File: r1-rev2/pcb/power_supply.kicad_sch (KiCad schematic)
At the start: 28 parts, among them J5 GT-BTP30003-xxxA-16A, Q3 AO3401A, U4 LM66100DCK, U5 TPS62A01DRLR, U6 TPS62A01DRLR, U7 AP2125K-3.0, U8 AP2125K-3.0, U9 TP4057

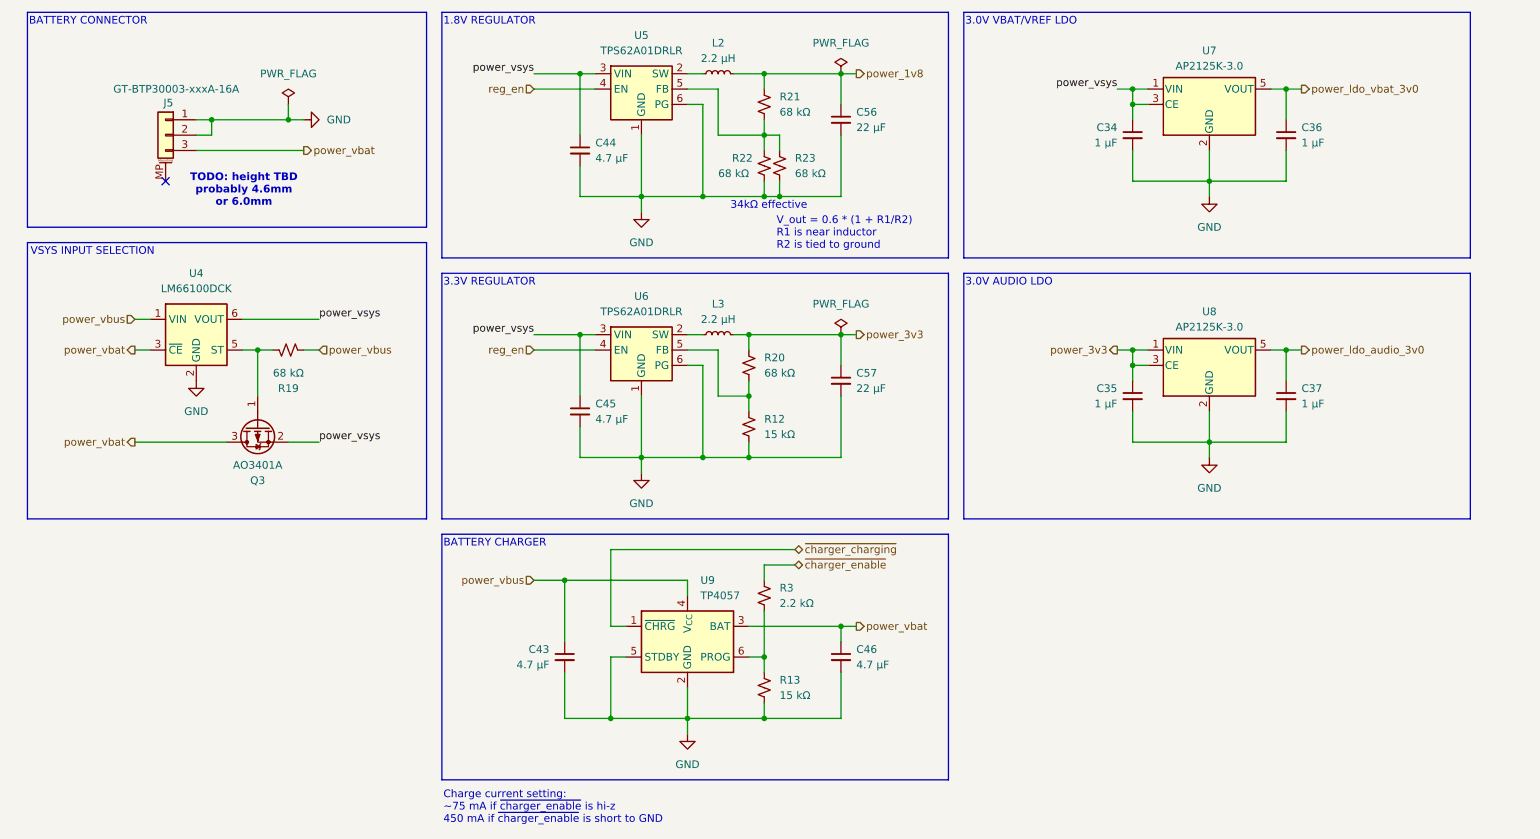
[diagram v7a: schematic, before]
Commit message: R1-Rev2: improve reset circuit, add XSPI CS pullup
Connect NRST to xspi_reset and the regulator power-good signals.
This should ensure that the STM32 and RAM will stay in reset
until both power rails have started up. It shouldn't be necessary
to control xspi_reset with a GPIO, but for now leave it connected
just in case.

The XSPI CS pin also requires an external pullup to guarantee it
will be pulled high during power-on, which is required to ensure
the RAM resets properly.
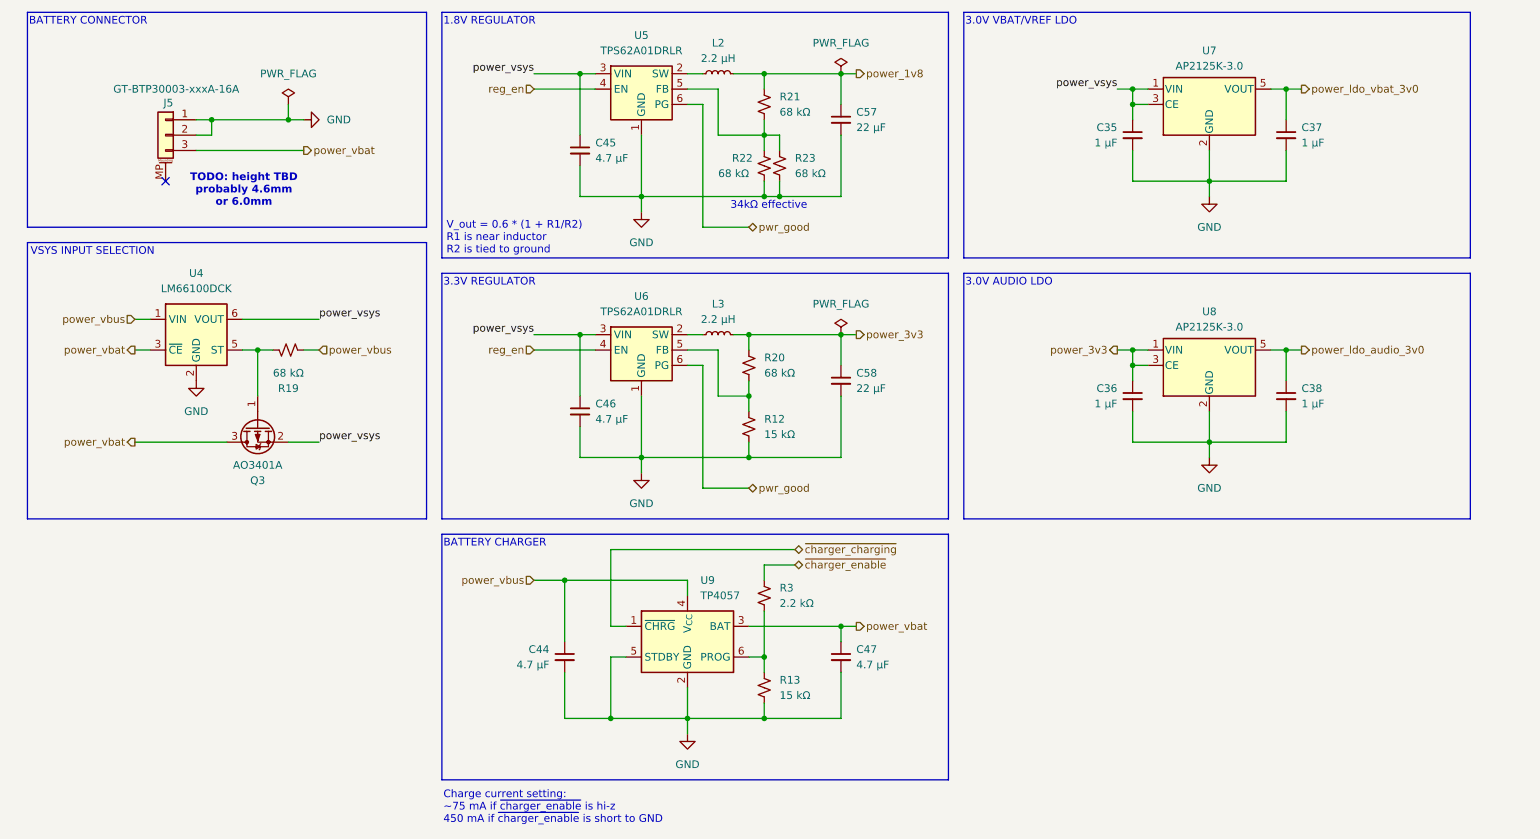
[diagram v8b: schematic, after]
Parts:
- renumbered C34 to C35, C35 to C36, C36 to C37, C37 to C38, C43 to C44, C44 to C45, C45 to C46, C46 to C47, C56 to C57, C57 to C58
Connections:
- net GND: no longer U5.6 (PG), U6.6 (PG)
- new net pwr_good: U5.6 (PG), U6.6 (PG)
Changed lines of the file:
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@@
 	(text "V_out = 0.6 * (1 + R1/R2)\nR1 is near inductor\nR2 is tied to ground"
 		(exclude_from_sim no)
-		(at 154.432 69.596 0)
+		(at 99.822 70.358 0)
 		(effects
 			(font
@@
 	)
 	(junction
-		(at 142.24 63.5)
-		(diameter 0)
-		(color 0 0 0 0)
-	)
-	(junction
-		(at 142.24 106.68)
-		(diameter 0)
-		(color 0 0 0 0)
-	)
-	(junction
 		(at 73.66 50.8)
 		(diameter 0)
@@
 	(wire
 		(pts
-			(xy 142.24 48.26) (xy 142.24 63.5)
-		)
-		(stroke
-			(width 0)
-			(type default)
-		)
-	)
-	(wire
-		(pts
 			(xy 226.06 60.96) (xy 238.76 60.96)
 		)
@@
 	(wire
 		(pts
+			(xy 142.24 91.44) (xy 142.24 111.76)
+		)
+		(stroke
+			(width 0)
+			(type default)
+		)
+	)
+	(wire
+		(pts
 			(xy 139.7 86.36) (xy 142.24 86.36)
 		)
@@
 	(wire
 		(pts
-			(xy 144.78 88.9) (xy 144.78 96.52)
+			(xy 142.24 48.26) (xy 142.24 68.58)
 		)
 		(stroke
@@
 	(wire
 		(pts
-			(xy 132.08 96.52) (xy 132.08 106.68)
+			(xy 144.78 88.9) (xy 144.78 96.52)
 		)
 		(stroke
@@
 	(wire
 		(pts
-			(xy 165.1 86.36) (xy 167.64 86.36)
+			(xy 132.08 96.52) (xy 132.08 106.68)
 		)
 		(stroke
@@
 	(wire
 		(pts
-			(xy 132.08 106.68) (xy 142.24 106.68)
+			(xy 165.1 86.36) (xy 167.64 86.36)
 		)
 		(stroke
@@
 	(wire
 		(pts
-			(xy 139.7 91.44) (xy 142.24 91.44)
+			(xy 132.08 106.68) (xy 149.86 106.68)
 		)
 		(stroke
@@
 	(wire
 		(pts
-			(xy 142.24 91.44) (xy 142.24 106.68)
+			(xy 139.7 91.44) (xy 142.24 91.44)
 		)
 		(stroke
@@
 	(wire
 		(pts
-			(xy 142.24 63.5) (xy 152.4 63.5)
+			(xy 132.08 63.5) (xy 152.4 63.5)
 		)
 		(stroke
@@
 	(wire
 		(pts
+			(xy 142.24 111.76) (xy 149.86 111.76)
+		)
+		(stroke
+			(width 0)
+			(type default)
+		)
+	)
+	(wire
+		(pts
 			(xy 139.7 127) (xy 139.7 129.54)
 		)
@@
 	(wire
 		(pts
-			(xy 142.24 106.68) (xy 149.86 106.68)
-		)
-		(stroke
-			(width 0)
-			(type default)
-		)
-	)
-	(wire
-		(pts
 			(xy 226.06 60.96) (xy 226.06 63.5)
 		)
@@
 	(wire
 		(pts
-			(xy 152.4 53.34) (xy 154.94 53.34)
+			(xy 142.24 68.58) (xy 149.86 68.58)
 		)
 		(stroke
@@
 	(wire
 		(pts
-			(xy 119.38 149.86) (xy 127 149.86)
+			(xy 152.4 53.34) (xy 154.94 53.34)
 		)
 		(stroke
@@
 	(wire
 		(pts
-			(xy 142.24 63.5) (xy 132.08 63.5)
+			(xy 119.38 149.86) (xy 127 149.86)
 		)
 		(stroke
@@
 		)
 	)
+	(hierarchical_label "pwr_good"
+		(shape tri_state)
+		(at 149.86 111.76 0)
+		(effects
+			(font
+				(size 1.27 1.27)
+			)
+			(justify left)
+		)
+	)
 	(hierarchical_label "power_vbus"
 		(shape input)
@@
 		)
 	)
+	(hierarchical_label "pwr_good"
+		(shape tri_state)
+		(at 149.86 68.58 0)
+		(effects
+			(font
+				(size 1.27 1.27)
+			)
+			(justify left)
+		)
+	)
 	(hierarchical_label "power_vbat"
 		(shape output)
@@
 		(on_board yes)
 		(dnp no)
-		(property "Reference" "C35"
+		(property "Reference" "C36"
 			(at 210.82 95.2562 0)
 			(effects
@@
 			(project "echo-r1"
 				(path "/aa241847-30f4-429d-a148-6a6e39ba98e0/48d39f5c-11a4-46cd-927a-56a9c6ae42fa"
-					(reference "C35")
+					(reference "C36")
 					(unit 1)
 				)
@@
 		(on_board yes)
 		(dnp no)
-		(property "Reference" "C57"
+		(property "Reference" "C58"
 			(at 167.64 92.7162 0)
 			(effects
@@
 			(project "echo-r1"
 				(path "/aa241847-30f4-429d-a148-6a6e39ba98e0/48d39f5c-11a4-46cd-927a-56a9c6ae42fa"
-					(reference "C57")
+					(reference "C58")
 					(unit 1)
 				)
@@
 		(on_board yes)
 		(dnp no)
-		(property "Reference" "C56"
+		(property "Reference" "C57"
 			(at 167.64 49.5362 0)
 			(effects
@@
 			(project "echo-r1"
 				(path "/aa241847-30f4-429d-a148-6a6e39ba98e0/48d39f5c-11a4-46cd-927a-56a9c6ae42fa"
-					(reference "C56")
+					(reference "C57")
 					(unit 1)
 				)
@@
 		(dnp no)
 		(fields_autoplaced yes)
-		(property "Reference" "C36"
+		(property "Reference" "C37"
 			(at 241.3 52.0762 0)
 			(effects
@@
 			(project ""
 				(path "/aa241847-30f4-429d-a148-6a6e39ba98e0/48d39f5c-11a4-46cd-927a-56a9c6ae42fa"
-					(reference "C36")
+					(reference "C37")
 					(unit 1)
 				)
@@
 		(on_board yes)
 		(dnp no)
-		(property "Reference" "C45"
+		(property "Reference" "C46"
 			(at 124.46 97.7962 0)
 			(effects
@@
 			(project ""
 				(path "/aa241847-30f4-429d-a148-6a6e39ba98e0/48d39f5c-11a4-46cd-927a-56a9c6ae42fa"
-					(reference "C45")
+					(reference "C46")
 					(unit 1)
 				)
@@
 		(on_board yes)
 		(dnp no)
-		(property "Reference" "C34"
+		(property "Reference" "C35"
 			(at 210.82 52.0762 0)
 			(effects
@@
 			(project "echo-r1"
 				(path "/aa241847-30f4-429d-a148-6a6e39ba98e0/48d39f5c-11a4-46cd-927a-56a9c6ae42fa"
-					(reference "C34")
+					(reference "C35")
 					(unit 1)
 				)
@@
 		(on_board yes)
 		(dnp no)
-		(property "Reference" "C44"
+		(property "Reference" "C45"
 			(at 124.46 54.6162 0)
 			(effects
@@
 			(project "echo-r1"
 				(path "/aa241847-30f4-429d-a148-6a6e39ba98e0/48d39f5c-11a4-46cd-927a-56a9c6ae42fa"
-					(reference "C44")
+					(reference "C45")
 					(unit 1)
 				)
@@
 		(on_board yes)
 		(dnp no)
-		(property "Reference" "C43"
+		(property "Reference" "C44"
 			(at 116.84 138.4362 0)
 			(effects
@@
 			(project "echo-r1"
 				(path "/aa241847-30f4-429d-a148-6a6e39ba98e0/48d39f5c-11a4-46cd-927a-56a9c6ae42fa"
-					(reference "C43")
+					(reference "C44")
 					(unit 1)
 				)
@@
 		(dnp no)
 		(fields_autoplaced yes)
-		(property "Reference" "C37"
+		(property "Reference" "C38"
 			(at 241.3 95.2562 0)
 			(effects
@@
 			(project "echo-r1"
 				(path "/aa241847-30f4-429d-a148-6a6e39ba98e0/48d39f5c-11a4-46cd-927a-56a9c6ae42fa"
-					(reference "C37")
+					(reference "C38")
 					(unit 1)
 				)
@@
 		(on_board yes)
 		(dnp no)
-		(property "Reference" "C46"
+		(property "Reference" "C47"
 			(at 167.64 138.4362 0)
 			(effects
@@
 			(project "echo-r1"
 				(path "/aa241847-30f4-429d-a148-6a6e39ba98e0/48d39f5c-11a4-46cd-927a-56a9c6ae42fa"
-					(reference "C46")
+					(reference "C47")
 					(unit 1)
 				)
